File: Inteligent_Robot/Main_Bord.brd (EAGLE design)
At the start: 160 x 107.6 mm, 83 parts, among them CN5 DF11-4DS-2C, CN6 DF11-4DS-2C, CN7 IL-G_ST_4, CN8 IL-G_ST_4, IC1 TWE-001L-IP, IC2 LTC2862A, IC5 A4988, IC7 A4988

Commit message: Complete_First_version
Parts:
- removed U$18: MCR03, ROHM:MCR03
- added R1: MCR006, ROHM:MCR006
- moved DC11 188.5 mm to (84.5, 8.83)
- moved C6 176.1 mm to (80.7, 7.11), turned to 270 degrees
- moved C4 170.3 mm to (87.5, 8.84), turned to 90 degrees
- moved DC10 168.8 mm to (85.9, 27.0)
- moved C7 167.1 mm to (62.9, 6.99), turned to 270 degrees
- moved DC12 162.0 mm to (65.5, 17.8)
- moved C3 155.6 mm to (88.6, 27.0), turned to 90 degrees
- moved U$15 153.5 mm to (75.9, 57.2), turned to 180 degrees
- moved C8 152.1 mm to (56.9, 33.8)
- moved U$14 150.2 mm to (78.7, 57.2), turned to 180 degrees
- moved RA4 145.9 mm to (58.9, 20.4), turned to 270 degrees
- moved C2 138.7 mm to (67.9, 19.5), turned to 90 degrees
- moved U$13 137.9 mm to (60.6, 38.0), turned to 180 degrees
- moved DC5 136.1 mm to (12.4, 13.3), turned to 270 degrees
- moved U$12 130.3 mm to (60.6, 42.1), turned to 180 degrees
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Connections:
- removed net DIR: IC5.P$19, IC7.P$19, R15.P$1, R7.P$1
- removed net MT_1A: IC5.P$24
- removed net MT_1B: IC5.P$21
- removed net MT_2A: IC5.P$26
- removed net MT_2B: IC5.P$1
- removed net N$47: DC11.P$1
- removed net STP: IC5.P$16, IC7.P$16, R14.P$1, R4.P$1
- removed net VCC: C26.P$1, C38.P$1, DC15.P$2, DC17.P$2, VR3.P$2, VR5.P$2
- net +5V: now also C26.P$1, C38.P$1, DC11.P$1, DC15.P$2, DC17.P$2, VR3.P$2, VR5.P$2
- net A*: now also DC3.P$2; no longer DC3.P$1
- net DIR1: now also IC5.P$19, R7.P$1; no longer RA1.P$2
- net DIR2: now also IC7.P$19, R15.P$1; no longer RA1.P$1
- net GND: no longer RA1.P$7, RA1.P$8, RA2.P$7, RA2.P$8, RA3.P$6
- net MT1_1A: now also CN7.P$3, IC5.P$24; no longer CN7.P$4
- net MT1_1B: now also CN7.P$4, IC5.P$21; no longer CN7.P$3
- net MT1_2A: now also IC5.P$26
- net MT1_2B: now also IC5.P$1
- net MT2_1A: now also CN8.P$3; no longer CN8.P$4
- net MT2_1B: now also CN8.P$4; no longer CN8.P$3
- net N$14: now also DC3.P$1, R1.P$1; no longer DC3.P$2, U$18.P$2
- net N$15: now also R1.P$2; no longer U$18.P$1
- net SLEEP1: no longer RA3.P$3
- net STP1: now also IC5.P$16, R4.P$1; no longer RA2.P$1
- net STP2: now also IC7.P$16, R14.P$1; no longer RA2.P$2
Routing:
- net GND: track 225.4 -> 862.9 mm, vias 22 -> 34
- net +5V: track 0.00 -> 302.4 mm, vias 0 -> 8
- net VDD: track 110.6 -> 398.8 mm, vias 6 -> 11
- net DIR2: track 0.00 -> 111.1 mm, vias 0 -> 4
- net STP2: track 0.00 -> 109.3 mm, vias 0 -> 2
- net +3.3V: track 0.00 -> 95.8 mm, vias 0 -> 4
- net STP1: track 0.00 -> 90.1 mm, vias 0 -> 4
- net SLEEP1: track 41.0 -> 129.0 mm, vias 2 -> 7
- net DIR1: track 0.00 -> 86.7 mm, vias 0 -> 1
- net M_TO_T-1: track 0.00 -> 68.2 mm
- net M_TO_T-2: track 0.00 -> 68.2 mm, vias 0 -> 2
- net VCC: track 66.1 -> 0.00 mm, vias 4 -> 0
- net DI: track 0.00 -> 62.5 mm, vias 0 -> 1
- net RO: track 0.00 -> 62.1 mm, vias 0 -> 3
- net SEL_485: track 0.00 -> 60.6 mm
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- added copper zone on layer 1, net GND
- added copper zone on layer 16, net GND
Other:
- board size 160 x 107.6 mm -> 132.1 x 101.6 mm

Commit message: Ver2
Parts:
- removed U$12, U$13, U$14, U$15: MCR03, ROHM:MCR03
- removed U$9: 16SVPS180M, OS-CON:SVCP_F8
- added C10, C9: GMR31, Murata:GMR31
- added DC-DC1: MPM01, SANKEN:MPM00_V
- added DC13: YFF21PC, TDK:YFF21PC
- added OS-CON1: 16SVPS180M, OS-CON:SVCP_F8
- added R10, R2, R5, R6, R9: MCR006, ROHM:MCR006
- DC1, DC2, DC3, DC4, DC6, DC7, DC9: value NFM3DPC223R1H3L -> YFF21PC; device Murata:NFM3DC -> TDK:YFF21PC
- moved C4 89.3 mm to (5.35, 43.9)
- moved DC-DC3 89.3 mm to (20.7, 53.6)
- moved DC11 82.2 mm to (8.77, 40.7), turned to 90 degrees
- moved DC1 66.0 mm to (91.6, 44.8), turned to 225 degrees
- moved C3 65.6 mm to (25.2, 43.8)
- moved DC-DC4 64.3 mm to (40.8, 53.7)
- moved DC10 58.4 mm to (29.0, 40.5), turned to 90 degrees
- moved C19 58.1 mm to (38.4, 6.77)
- moved DC2 52.7 mm to (73.2, 44.7), turned to 225 degrees
- moved DC8 46.7 mm to (30.1, 18.6), turned to 225 degrees
- moved CN4 40.7 mm to (37.4, 18.2), turned to 270 degrees
- moved C34 36.1 mm to (83.9, 53.3)
- moved C35 36.1 mm to (82.2, 48.8)
- moved C36 36.1 mm to (82.2, 49.9)
- moved C39 36.1 mm to (87.4, 53.3)
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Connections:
- new net +7.5V: C6.P$1, C7.P$1, CN5.P$3, CN6.P$3, DC13.P$2
- new net N$6: C9.P$1, DC-DC1.P$5, DC-DC1.P$6, DC-DC1.P$7, DC13.P$1
- new net N$9: DC-DC1.P$4, R10.P$1
- net +5V: now also DC6.P$1, R2.P$1, R5.P$1, R6.P$1, R9.P$1; no longer DC8.P$1, U$12.P$1, U$13.P$1, U$14.P$1, U$15.P$1
- net A*: now also DC4.P$1; no longer DC3.P$2
- net B*: now also DC3.P$2; no longer DC4.P$1
- net GND: now also C10.P$2, C9.P$2, DC-DC1.P$1, DC-DC1.P$3, DC1.GND1, DC1.GND2, DC13.GND1, DC13.GND2, DC2.GND1, DC2.GND2, DC3.GND1, DC3.GND2, DC4.GND1, DC4.GND2, DC6.GND1, DC6.GND2, DC7.GND1, DC7.GND2, DC9.GND1, DC9.GND2, OS-CON1.P$1, R10.P$2; no longer DC1.P$3, DC1.P$4, DC2.P$3, DC2.P$4, DC3.P$3, DC3.P$4, DC4.P$3, DC4.P$4, DC6.P$3, DC6.P$4, DC7.P$3, DC7.P$4, DC9.P$3, DC9.P$4, U$9.P$1
- net MOTOR_INT: now also RA3.P$1; no longer RA3.P$2
- net MS1: now also KIT1.P$16
- net MS2: now also KIT1.P$17
- net MS3: now also KIT1.P$19
- net M_TO_T-1: now also DC9.P$1; no longer DC6.P$2
- net M_TO_T-2: now also DC8.P$1; no longer DC7.P$2
- net N$1: now also RA2.P$3; no longer RA2.P$4
- net N$14: now also DC4.P$2; no longer DC3.P$1
- net N$15: now also DC3.P$1; no longer DC4.P$2
- net N$2: now also RA2.P$4; no longer RA2.P$3
- net N$3: now also DC6.P$2; no longer DC8.P$2
- net N$36: now also DC2.P$2; no longer DC1.P$1
- net N$37: now also DC1.P$2; no longer DC2.P$1
- net N$38: now also R9.P$2; no longer U$12.P$2
- net N$39: now also R6.P$2; no longer U$13.P$2
- net N$40: now also R2.P$2; no longer U$14.P$2
- net N$41: now also R5.P$2; no longer U$15.P$2
- net N$5: now also DC7.P$2; no longer DC9.P$1
- net N$7: now also RA1.P$3; no longer RA1.P$4
- net N$8: now also RA1.P$4; no longer RA1.P$3
- net PSD: now also DC7.P$1; no longer DC9.P$2
- net RT-T: now also DC8.P$2; no longer DC7.P$1
- net SEL_485: now also RA3.P$2; no longer RA3.P$1
- net STP1: now also DC2.P$1; no longer DC1.P$2
- net STP2: now also DC1.P$1; no longer DC2.P$2
- net TX-T: now also DC9.P$2; no longer DC6.P$1
- net VDD: now also C10.P$1, DC-DC1.P$2, OS-CON1.P$2+; no longer C6.P$1, C7.P$1, CN5.P$3, CN6.P$3, U$9.P$2+
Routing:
- net N$1: track 49.3 -> 174.1 mm
- net N$2: track 46.9 -> 169.9 mm
- net STP2: track 109.3 -> 7.29 mm
- net N$37: track 5.08 -> 89.5 mm, vias 0 -> 1
- net STP1: track 90.1 -> 7.15 mm, vias 4 -> 2
- net +7.5V: track 0.00 -> 65.4 mm, vias 0 -> 3
- net GND: track 862.9 -> 919.3 mm, vias 34 -> 30
- net M_TO_T-1: track 68.2 -> 16.2 mm, vias 0 -> 1
- net SLEEP1: track 129.0 -> 77.1 mm
- net MS1: track 9.17 -> 57.5 mm, vias 2 -> 5
- net N$36: track 5.61 -> 51.1 mm, vias 0 -> 3
- net +3.3V: track 95.8 -> 141.2 mm, vias 4 -> 5
- net MS2: track 10.6 -> 54.3 mm, vias 2 -> 5
- net MS3: track 8.81 -> 51.3 mm, vias 0 -> 4
- net M_TO_T-2: track 68.2 -> 29.2 mm
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- removed copper zone on layer 1, net GND
- removed copper zone on layer 16, net GND
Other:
- board size 132.1 x 101.6 mm -> 119.4 x 71.7 mm

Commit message: update
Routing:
- net GND: track 919.3 -> 921.7 mm
- net N$1: track 174.1 -> 175.1 mm

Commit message: Refime pisitions
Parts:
- added 0R1, 0R2: 5106, Keystone:5106JUMP_0805
- moved C9 45.8 mm to (63.7, 19.3), turned to 0 degrees
- moved DC13 43.8 mm to (63.7, 15.4)
- moved R10 41.5 mm to (67.8, 24.5), turned to 90 degrees
- moved CN3 36.2 mm to (34.6, 20.3)
- moved DC12 35.9 mm to (47.1, 16.6)
- moved DC4 35.9 mm to (42.9, 14.2)
- moved IC2 35.9 mm to (44.4, 19.2)
- moved DC3 35.9 mm to (45.7, 14.2)
- moved R1 35.9 mm to (44.1, 17.1)
- moved C2 35.8 mm to (49.5, 19.1), turned to 0 degrees
- moved CN1 33.0 mm to (25.5, 17.8)
- moved CN2 33.0 mm to (16.7, 17.7)
- moved R6 33.0 mm to (20.8, 17.7)
- moved R9 33.0 mm to (20.8, 20.2)
- moved IC1 32.8 mm to (8.49, 50.9)
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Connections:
- new net N$10: 0R2.P$2, CN1.3
- new net N$11: 0R1.P$2, CN1.2
- net N$1: now also 0R2.P$1; no longer CN1.2
- net N$2: now also 0R1.P$1; no longer CN1.3
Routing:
- net +5V: track 332.4 -> 156.0 mm, vias 9 -> 2
- net N$1: track 175.1 -> 8.37 mm, vias 1 -> 0
- net N$2: track 169.9 -> 8.23 mm, vias 1 -> 0
- net GND: track 921.7 -> 781.2 mm, vias 30 -> 33
- net N$10: track 0.00 -> 107.5 mm
- net N$11: track 0.00 -> 102.4 mm
- net VDD: track 427.7 -> 339.8 mm
- net +3.3V: track 141.2 -> 63.1 mm, vias 5 -> 4
- net +7.5V: track 65.4 -> 29.9 mm, vias 3 -> 0
- net SEL_485: track 61.7 -> 28.8 mm
- net RO: track 50.7 -> 20.2 mm
- net DI: track 50.6 -> 20.9 mm, vias 1 -> 0
- net RST: track 6.60 -> 30.9 mm, vias 0 -> 1
- net PSD: track 35.2 -> 14.2 mm, vias 1 -> 0
- net M_TO_T-2: track 29.2 -> 16.2 mm, vias 2 -> 1
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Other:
- board size 119.4 x 71.7 mm -> 120.7 x 71.7 mm

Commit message: Refine finshed
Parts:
- moved DC17 0.30 mm to (91.3, 47.2)
- moved DC15 0.30 mm to (72.9, 47.0)
- moved R13 0.20 mm to (96.0, 57.2)
- moved R3 0.20 mm to (77.6, 57.0)
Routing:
- net +5V: track 156.0 -> 329.4 mm, vias 2 -> 9
- net GND: track 781.2 -> 908.1 mm
- net VDD: track 339.8 -> 401.6 mm
- net A*: track 33.5 -> 31.9 mm
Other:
- board size 120.7 x 71.7 mm -> 109 x 74.2 mm

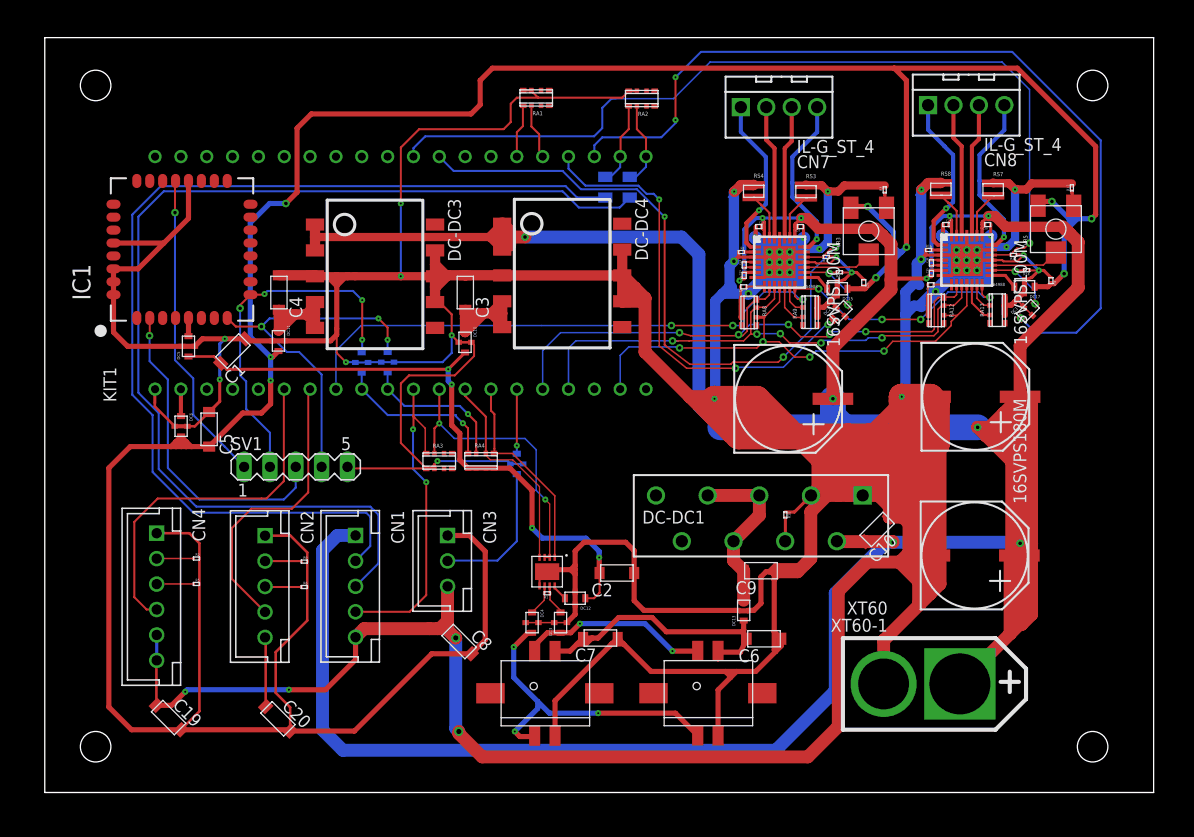
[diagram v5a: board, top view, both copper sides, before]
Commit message: Add Groung  solid pattern
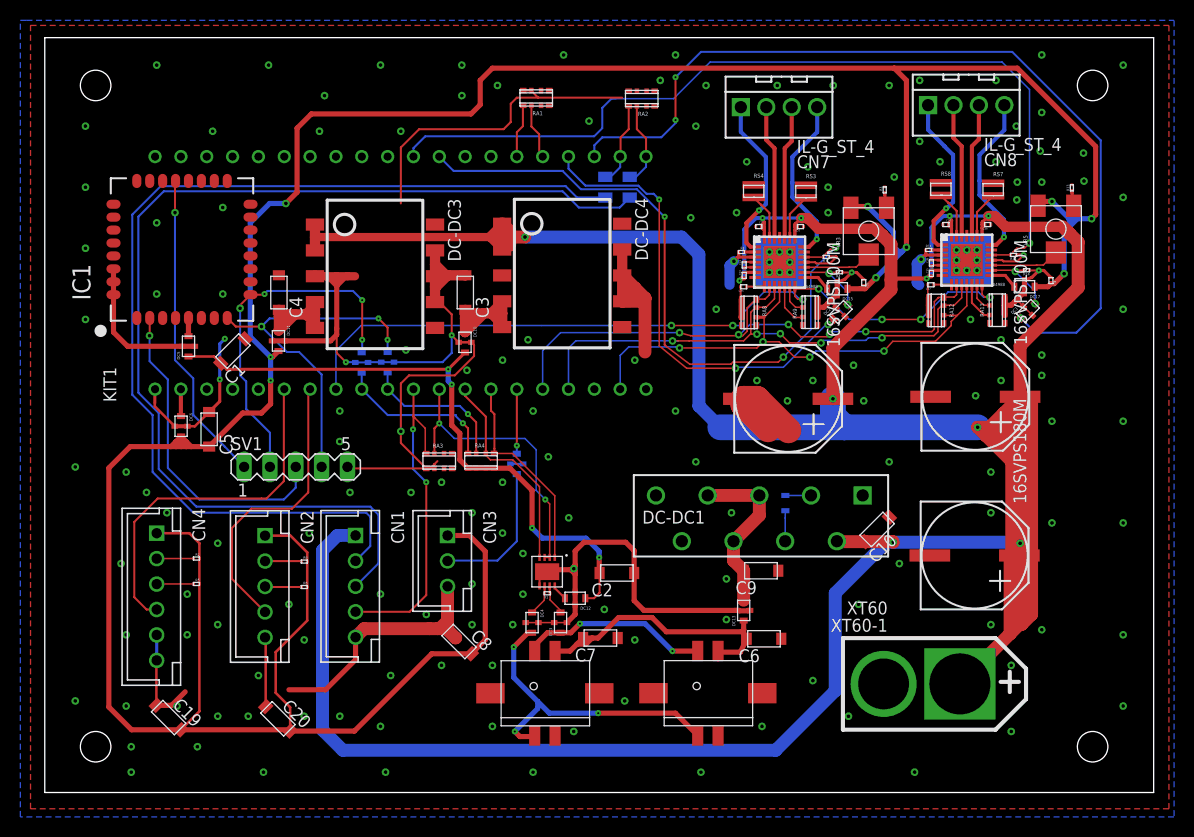
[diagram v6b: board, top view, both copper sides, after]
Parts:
- R10: value MCR006 -> MCR03; device ROHM:MCR006 -> ROHM:MCR03
- moved R10 0.70 mm to (67.8, 25.2), flipped to the bottom
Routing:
- net GND: track 908.1 -> 317.5 mm, vias 33 -> 160
- net N$9: track 2.31 -> 3.00 mm
- added copper zone on layer 1, net GND
- added copper zone on layer 16, net GND
